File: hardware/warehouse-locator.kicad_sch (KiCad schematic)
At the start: 8 parts, among them J1 Screw_Terminal_01x03, J2 Screw_Terminal_01x03, J3 Screw_Terminal_01x03, J4 Barrel_Jack, J5 Screw_Terminal_01x03, J6 Screw_Terminal_01x03, J7 Screw_Terminal_01x03, U1 ESP32-DevKitC

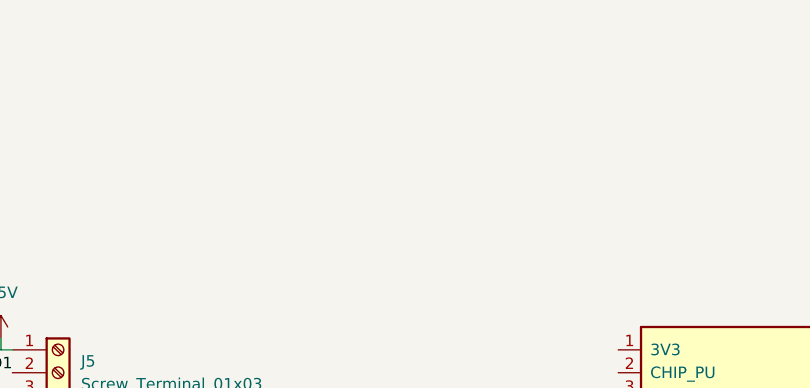
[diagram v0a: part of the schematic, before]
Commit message: Ethernet header
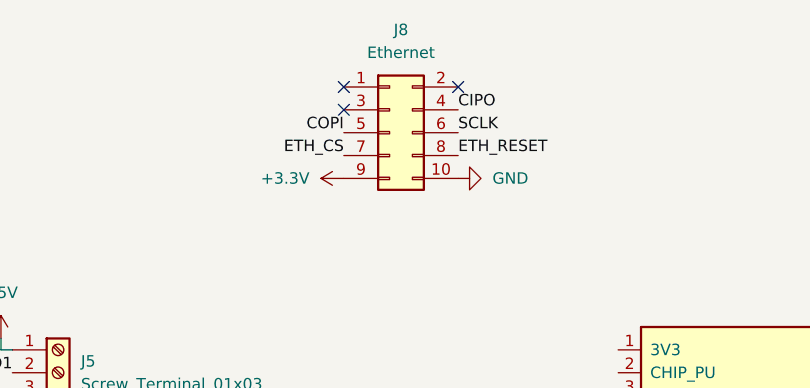
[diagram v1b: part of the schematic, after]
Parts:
- added J8: Ethernet, Connector_PinSocket_2.54mm:PinSocket_2x05_P2.54mm_Vertical, symbol Connector_Generic:Conn_02x05_Odd_Even
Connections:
- net GND: now also J8.10 (Pin_10)
- new net +3.3V: J8.9 (Pin_9)
- new net CIPO: J8.4 (Pin_4)
- new net COPI: J8.5 (Pin_5)
- new net ETH_CS: J8.7 (Pin_7)
- new net ETH_RESET: J8.8 (Pin_8)
- new net SCLK: J8.6 (Pin_6)
- no-connect marks 0 -> 3
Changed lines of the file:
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@@
 (kicad_sch (version 20211123) (generator eeschema)
   (paper "A4")
+  (no_connect (at 134.62 54.61))
+  (no_connect (at 134.62 52.07))
+  (no_connect (at 147.32 52.07))
   (wire (pts (xy 96.52 81.28) (xy 97.79 81.28))
     (stroke (width 0) (type default) (color 0 0 0 0))
@@
     (effects (font (size 1.27 1.27)) (justify right bottom))
   )
+  (label "ETH_RESET" (at 147.32 59.69 0)
+    (effects (font (size 1.27 1.27)) (justify left bottom))
+  )
+  (label "ETH_CS" (at 134.62 59.69 180)
+    (effects (font (size 1.27 1.27)) (justify right bottom))
+  )
+  (label "CIPO" (at 147.32 54.61 0)
+    (effects (font (size 1.27 1.27)) (justify left bottom))
+  )
   (label "LED0" (at 60.96 83.82 180)
     (effects (font (size 1.27 1.27)) (justify right bottom))
@@
   (label "LED5" (at 97.79 127 180)
     (effects (font (size 1.27 1.27)) (justify right bottom))
+  )
+  (label "COPI" (at 134.62 57.15 180)
+    (effects (font (size 1.27 1.27)) (justify right bottom))
+  )
+  (label "SCLK" (at 147.32 57.15 0)
+    (effects (font (size 1.27 1.27)) (justify left bottom))
+  )
+  (symbol (lib_id "power:+3.3V") (at 134.62 62.23 90) (unit 1)
+    (in_bom yes) (on_board yes) (fields_autoplaced)
+    (property "Reference" "#PWR015" (id 0) (at 138.43 62.23 0)
+      (effects (font (size 1.27 1.27)) hide)
+    )
+    (property "Value" "+3.3V" (id 1) (at 130.81 62.2299 90)
+      (effects (font (size 1.27 1.27)) (justify left))
+    )
+    (property "Footprint" "" (id 2) (at 134.62 62.23 0)
+      (effects (font (size 1.27 1.27)) hide)
+    )
+    (property "Datasheet" "" (id 3) (at 134.62 62.23 0)
+      (effects (font (size 1.27 1.27)) hide)
+    )
+    (pin "1")
   )
   (symbol (lib_id "power:+5V") (at 96.52 80.01 0) (unit 1)
@@
     (pin "3")
   )
+  (symbol (lib_id "power:GND") (at 147.32 62.23 90) (unit 1)
+    (in_bom yes) (on_board yes) (fields_autoplaced)
+    (property "Reference" "#PWR016" (id 0) (at 153.67 62.23 0)
+      (effects (font (size 1.27 1.27)) hide)
+    )
+    (property "Value" "GND" (id 1) (at 151.13 62.2299 90)
+      (effects (font (size 1.27 1.27)) (justify right))
+    )
+    (property "Footprint" "" (id 2) (at 147.32 62.23 0)
+      (effects (font (size 1.27 1.27)) hide)
+    )
+    (property "Datasheet" "" (id 3) (at 147.32 62.23 0)
+      (effects (font (size 1.27 1.27)) hide)
+    )
+    (pin "1")
+  )
   (symbol (lib_id "Connector:Screw_Terminal_01x03") (at 102.87 127 0) (unit 1)
     (in_bom yes) (on_board yes) (fields_autoplaced)
@@
     )
     (pin "1")
+  )
+  (symbol (lib_id "Connector_Generic:Conn_02x05_Odd_Even") (at 139.7 57.15 0) (unit 1)
+    (in_bom yes) (on_board yes) (fields_autoplaced)
+    (property "Reference" "J8" (id 0) (at 140.97 45.72 0))
+    (property "Value" "Ethernet" (id 1) (at 140.97 48.26 0))
+    (property "Footprint" "Connector_PinSocket_2.54mm:PinSocket_2x05_P2.54mm_Vertical" (id 2) (at 139.7 57.15 0)
+      (effects (font (size 1.27 1.27)) hide)
+    )
+    (property "Datasheet" "~" (id 3) (at 139.7 57.15 0)
+      (effects (font (size 1.27 1.27)) hide)
+    )
+    (pin "1")
+    (pin "10")
+    (pin "2")
+    (pin "3")
+    (pin "4")
+    (pin "5")
+    (pin "6")
+    (pin "7")
+    (pin "8")
+    (pin "9")
   )
   (symbol (lib_id "power:GND") (at 59.69 109.22 0) (unit 1)
@@
       (reference "#PWR014") (unit 1) (value "GND") (footprint "")
     )
+    (path "/053d9fce-626c-4602-916b-ef89efbc2685"
+      (reference "#PWR015") (unit 1) (value "+3.3V") (footprint "")
+    )
+    (path "/c6e94d68-e716-4c42-b935-ba265a888be2"
+      (reference "#PWR016") (unit 1) (value "GND") (footprint "")
+    )
     (path "/3aaacb84-122f-4340-95d3-0bf04eee80d2"
       (reference "J1") (unit 1) (value "Screw_Terminal_01x03") (footprint "TerminalBlock_Phoenix:TerminalBlock_Phoenix_MKDS-1,5-3_1x03_P5.00mm_Horizontal")
@@
       (reference "J7") (unit 1) (value "Screw_Terminal_01x03") (footprint "TerminalBlock_Phoenix:TerminalBlock_Phoenix_MKDS-1,5-3_1x03_P5.00mm_Horizontal")
     )
+    (path "/df94ba07-cbc6-4baa-93b8-732ae39550c6"
+      (reference "J8") (unit 1) (value "Ethernet") (footprint "Connector_PinSocket_2.54mm:PinSocket_2x05_P2.54mm_Vertical")
+    )
     (path "/8a6d48a6-b7bb-4a02-b51b-9f669ac7dca2"

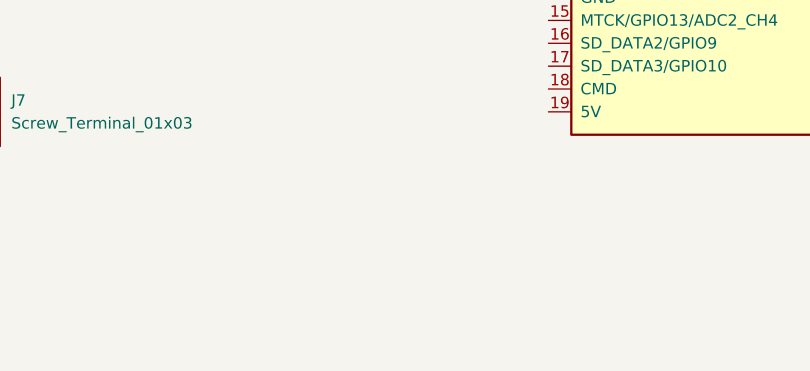
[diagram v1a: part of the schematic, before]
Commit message: Component positioning
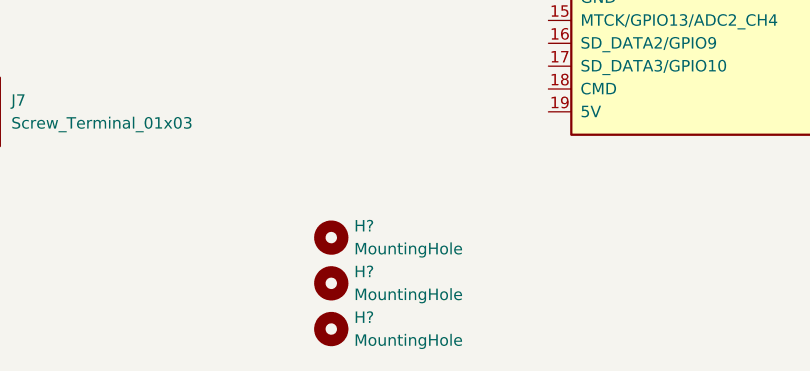
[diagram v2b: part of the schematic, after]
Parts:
- added H? (x3): MountingHole, MountingHole:MountingHole_3.2mm_M3_DIN965_Pad, symbol Mechanical:MountingHole
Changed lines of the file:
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@@
     (pin "3")
+  )
+  (symbol (lib_id "Mechanical:MountingHole") (at 140.97 140.97 0) (unit 1)
+    (in_bom yes) (on_board yes) (fields_autoplaced)
+    (property "Reference" "H?" (id 0) (at 143.51 139.6999 0)
+      (effects (font (size 1.27 1.27)) (justify left))
+    )
+    (property "Value" "MountingHole" (id 1) (at 143.51 142.2399 0)
+      (effects (font (size 1.27 1.27)) (justify left))
+    )
+    (property "Footprint" "MountingHole:MountingHole_3.2mm_M3_DIN965_Pad" (id 2) (at 140.97 140.97 0)
+      (effects (font (size 1.27 1.27)) hide)
+    )
+    (property "Datasheet" "~" (id 3) (at 140.97 140.97 0)
+      (effects (font (size 1.27 1.27)) hide)
+    )
   )
   (symbol (lib_id "power:+5V") (at 59.69 101.6 0) (unit 1)
@@
     (pin "1")
   )
+  (symbol (lib_id "Mechanical:MountingHole") (at 140.97 151.13 0) (unit 1)
+    (in_bom yes) (on_board yes) (fields_autoplaced)
+    (property "Reference" "H?" (id 0) (at 143.51 149.8599 0)
+      (effects (font (size 1.27 1.27)) (justify left))
+    )
+    (property "Value" "MountingHole" (id 1) (at 143.51 152.3999 0)
+      (effects (font (size 1.27 1.27)) (justify left))
+    )
+    (property "Footprint" "MountingHole:MountingHole_3.2mm_M3_DIN965_Pad" (id 2) (at 140.97 151.13 0)
+      (effects (font (size 1.27 1.27)) hide)
+    )
+    (property "Datasheet" "~" (id 3) (at 140.97 151.13 0)
+      (effects (font (size 1.27 1.27)) hide)
+    )
+  )
   (symbol (lib_id "Connector:Screw_Terminal_01x03") (at 66.04 127 0) (unit 1)
     (in_bom yes) (on_board yes) (fields_autoplaced)
@@
     (pin "2")
     (pin "3")
+  )
+  (symbol (lib_id "Mechanical:MountingHole") (at 140.97 146.05 0) (unit 1)
+    (in_bom yes) (on_board yes) (fields_autoplaced)
+    (property "Reference" "H?" (id 0) (at 143.51 144.7799 0)
+      (effects (font (size 1.27 1.27)) (justify left))
+    )
+    (property "Value" "MountingHole" (id 1) (at 143.51 147.3199 0)
+      (effects (font (size 1.27 1.27)) (justify left))
+    )
+    (property "Footprint" "MountingHole:MountingHole_3.2mm_M3_DIN965_Pad" (id 2) (at 140.97 146.05 0)
+      (effects (font (size 1.27 1.27)) hide)
+    )
+    (property "Datasheet" "~" (id 3) (at 140.97 146.05 0)
+      (effects (font (size 1.27 1.27)) hide)
+    )
   )
   (symbol (lib_id "Connector:Screw_Terminal_01x03") (at 66.04 105.41 0) (unit 1)
@@
       (reference "#PWR016") (unit 1) (value "GND") (footprint "")
     )
+    (path "/3f6f5fd4-bf84-4f5a-b527-b698f4821ee8"
+      (reference "H?") (unit 1) (value "MountingHole") (footprint "MountingHole:MountingHole_3.2mm_M3_DIN965_Pad")
+    )
+    (path "/a523383e-b510-4a6d-92cb-0d2f830ea5c3"
+      (reference "H?") (unit 1) (value "MountingHole") (footprint "MountingHole:MountingHole_3.2mm_M3_DIN965_Pad")
+    )
+    (path "/a915c05e-ae38-4c6d-9a9c-84e50169004a"
+      (reference "H?") (unit 1) (value "MountingHole") (footprint "MountingHole:MountingHole_3.2mm_M3_DIN965_Pad")
+    )
     (path "/3aaacb84-122f-4340-95d3-0bf04eee80d2"

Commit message: Pins connected
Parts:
- gave numbers to parts that had none: 3
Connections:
- net +3.3V: now also U1.1 (3V3)
- net +5V: now also U1.19 (5V)
- net CIPO: now also U1.31 (GPIO19)
- net COPI: now also U1.37 (GPIO23)
- net ETH_CS: now also U1.29 (*GPIO5)
- net GND: now also U1.14 (GND), U1.32 (GND), U1.38 (GND)
- net LED0: now also U1.33 (GPIO21)
- net LED1: now also U1.28 (GPIO17)
- net LED2: now also U1.26 (ADC2_CH0/GPIO4)
- net LED3: now also U1.36 (GPIO22)
- net LED4: now also U1.27 (GPIO16)
- net LED5: now also U1.24 (ADC2_CH2/*GPIO2)
- net SCLK: now also U1.30 (GPIO18)
- net ETH_RESET: no longer names the net of J8.8 (Pin_8)
- no-connect marks 3 -> 27
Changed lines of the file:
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@@
 (kicad_sch (version 20211123) (generator eeschema)
   (paper "A4")
+  (no_connect (at 165.1 116.84))
+  (no_connect (at 233.68 124.46))
+  (no_connect (at 165.1 119.38))
+  (no_connect (at 165.1 83.82))
   (no_connect (at 134.62 54.61))
+  (no_connect (at 165.1 99.06))
   (no_connect (at 134.62 52.07))
+  (no_connect (at 165.1 124.46))
+  (no_connect (at 233.68 127))
+  (no_connect (at 233.68 121.92))
+  (no_connect (at 165.1 93.98))
+  (no_connect (at 165.1 121.92))
+  (no_connect (at 165.1 104.14))
+  (no_connect (at 165.1 91.44))
+  (no_connect (at 233.68 114.3))
+  (no_connect (at 233.68 119.38))
+  (no_connect (at 165.1 86.36))
+  (no_connect (at 233.68 91.44))
+  (no_connect (at 165.1 101.6))
+  (no_connect (at 165.1 96.52))
+  (no_connect (at 165.1 88.9))
+  (no_connect (at 147.32 59.69))
+  (no_connect (at 165.1 111.76))
   (no_connect (at 147.32 52.07))
+  (no_connect (at 165.1 109.22))
+  (no_connect (at 165.1 106.68))
+  (no_connect (at 233.68 88.9))
   (wire (pts (xy 96.52 81.28) (xy 97.79 81.28))
     (stroke (width 0) (type default) (color 0 0 0 0))
@@
     (stroke (width 0) (type default) (color 0 0 0 0))
   )
+  (wire (pts (xy 238.76 96.52) (xy 233.68 96.52))
+    (stroke (width 0) (type default) (color 0 0 0 0))
+  )
   (wire (pts (xy 96.52 101.6) (xy 96.52 102.87))
     (stroke (width 0) (type default) (color 0 0 0 0))
@@
   )
   (wire (pts (xy 59.69 129.54) (xy 60.96 129.54))
+    (stroke (width 0) (type default) (color 0 0 0 0))
+  )
+  (wire (pts (xy 238.76 81.28) (xy 233.68 81.28))
     (stroke (width 0) (type default) (color 0 0 0 0))
   )
@@
     (effects (font (size 1.27 1.27)) (justify right bottom))
   )
+  (label "LED1" (at 233.68 106.68 0)
+    (effects (font (size 1.27 1.27)) (justify left bottom))
+  )
+  (label "LED0" (at 233.68 93.98 0)
+    (effects (font (size 1.27 1.27)) (justify left bottom))
+  )
   (label "LED3" (at 97.79 105.41 180)
     (effects (font (size 1.27 1.27)) (justify right bottom))
   )
+  (label "CIPO" (at 233.68 99.06 0)
+    (effects (font (size 1.27 1.27)) (justify left bottom))
+  )
   (label "LED1" (at 97.79 83.82 180)
     (effects (font (size 1.27 1.27)) (justify right bottom))
@@
     (effects (font (size 1.27 1.27)) (justify right bottom))
   )
-  (label "ETH_RESET" (at 147.32 59.69 0)
+  (label "LED2" (at 233.68 111.76 0)
+    (effects (font (size 1.27 1.27)) (justify left bottom))
+  )
+  (label "LED4" (at 233.68 109.22 0)
     (effects (font (size 1.27 1.27)) (justify left bottom))
   )
@@
     (effects (font (size 1.27 1.27)) (justify left bottom))
   )
+  (label "COPI" (at 233.68 83.82 0)
+    (effects (font (size 1.27 1.27)) (justify left bottom))
+  )
   (label "LED0" (at 60.96 83.82 180)
     (effects (font (size 1.27 1.27)) (justify right bottom))
   )
+  (label "SCLK" (at 233.68 101.6 0)
+    (effects (font (size 1.27 1.27)) (justify left bottom))
+  )
+  (label "LED5" (at 233.68 116.84 0)
+    (effects (font (size 1.27 1.27)) (justify left bottom))
+  )
+  (label "LED3" (at 233.68 86.36 0)
+    (effects (font (size 1.27 1.27)) (justify left bottom))
+  )
   (label "LED5" (at 97.79 127 180)
     (effects (font (size 1.27 1.27)) (justify right bottom))
   )
+  (label "ETH_CS" (at 233.68 104.14 0)
+    (effects (font (size 1.27 1.27)) (justify left bottom))
+  )
   (label "COPI" (at 134.62 57.15 180)
     (effects (font (size 1.27 1.27)) (justify right bottom))
@@
     (effects (font (size 1.27 1.27)) (justify left bottom))
   )
+  (symbol (lib_id "power:+5V") (at 165.1 127 90) (unit 1)
+    (in_bom yes) (on_board yes)
+    (property "Reference" "#PWR?" (id 0) (at 168.91 127 0)
+      (effects (font (size 1.27 1.27)) hide)
+    )
+    (property "Value" "+5V" (id 1) (at 157.48 127 90)
+      (effects (font (size 1.27 1.27)) (justify right))
+    )
+    (property "Footprint" "" (id 2) (at 165.1 127 0)
+      (effects (font (size 1.27 1.27)) hide)
+    )
+    (property "Datasheet" "" (id 3) (at 165.1 127 0)
+      (effects (font (size 1.27 1.27)) hide)
+    )
+    (pin "1")
+  )
   (symbol (lib_id "power:+3.3V") (at 134.62 62.23 90) (unit 1)
     (in_bom yes) (on_board yes) (fields_autoplaced)
@@
     )
     (property "Datasheet" "" (id 3) (at 134.62 62.23 0)
+      (effects (font (size 1.27 1.27)) hide)
+    )
+    (pin "1")
+  )
+  (symbol (lib_name "GND_2") (lib_id "power:GND") (at 165.1 114.3 270) (unit 1)
+    (in_bom yes) (on_board yes) (fields_autoplaced)
+    (property "Reference" "#PWR?" (id 0) (at 158.75 114.3 0)
+      (effects (font (size 1.27 1.27)) hide)
+    )
+    (property "Value" "GND" (id 1) (at 161.29 114.2999 90)
+      (effects (font (size 1.27 1.27)) (justify right))
+    )
+    (property "Footprint" "" (id 2) (at 165.1 114.3 0)
+      (effects (font (size 1.27 1.27)) hide)
+    )
+    (property "Datasheet" "" (id 3) (at 165.1 114.3 0)
       (effects (font (size 1.27 1.27)) hide)
     )
@@
     (pin "3")
   )
+  (symbol (lib_name "GND_1") (lib_id "power:GND") (at 238.76 81.28 90) (unit 1)
+    (in_bom yes) (on_board yes) (fields_autoplaced)
+    (property "Reference" "#PWR?" (id 0) (at 245.11 81.28 0)
+      (effects (font (size 1.27 1.27)) hide)
+    )
+    (property "Value" "GND" (id 1) (at 242.57 81.2799 90)
+      (effects (font (size 1.27 1.27)) (justify right))
+    )
+    (property "Footprint" "" (id 2) (at 238.76 81.28 0)
+      (effects (font (size 1.27 1.27)) hide)
+    )
+    (property "Datasheet" "" (id 3) (at 238.76 81.28 0)
+      (effects (font (size 1.27 1.27)) hide)
+    )
+    (pin "1")
+  )
   (symbol (lib_id "Connector:Screw_Terminal_01x03") (at 66.04 83.82 0) (unit 1)
     (in_bom yes) (on_board yes) (fields_autoplaced)
@@
   (symbol (lib_id "Mechanical:MountingHole") (at 140.97 140.97 0) (unit 1)
     (in_bom yes) (on_board yes) (fields_autoplaced)
-    (property "Reference" "H?" (id 0) (at 143.51 139.6999 0)
+    (property "Reference" "H1" (id 0) (at 143.51 139.6999 0)
       (effects (font (size 1.27 1.27)) (justify left))
     )
@@
   (symbol (lib_id "Mechanical:MountingHole") (at 140.97 151.13 0) (unit 1)
     (in_bom yes) (on_board yes) (fields_autoplaced)
-    (property "Reference" "H?" (id 0) (at 143.51 149.8599 0)
+    (property "Reference" "H3" (id 0) (at 143.51 149.8599 0)
       (effects (font (size 1.27 1.27)) (justify left))
     )
@@
   (symbol (lib_id "Mechanical:MountingHole") (at 140.97 146.05 0) (unit 1)
     (in_bom yes) (on_board yes) (fields_autoplaced)
-    (property "Reference" "H?" (id 0) (at 143.51 144.7799 0)
+    (property "Reference" "H2" (id 0) (at 143.51 144.7799 0)
       (effects (font (size 1.27 1.27)) (justify left))
     )
@@
     (pin "2")
     (pin "3")
+  )
+  (symbol (lib_name "GND_1") (lib_id "power:GND") (at 238.76 96.52 90) (unit 1)
+    (in_bom yes) (on_board yes) (fields_autoplaced)
+    (property "Reference" "#PWR?" (id 0) (at 245.11 96.52 0)
+      (effects (font (size 1.27 1.27)) hide)
+    )
+    (property "Value" "GND" (id 1) (at 242.57 96.5199 90)
+      (effects (font (size 1.27 1.27)) (justify right))
+    )
+    (property "Footprint" "" (id 2) (at 238.76 96.52 0)
+      (effects (font (size 1.27 1.27)) hide)
+    )
+    (property "Datasheet" "" (id 3) (at 238.76 96.52 0)
+      (effects (font (size 1.27 1.27)) hide)
+    )
+    (pin "1")
+  )
+  (symbol (lib_id "power:+3.3V") (at 165.1 81.28 90) (unit 1)
+    (in_bom yes) (on_board yes) (fields_autoplaced)
+    (property "Reference" "#PWR?" (id 0) (at 168.91 81.28 0)
+      (effects (font (size 1.27 1.27)) hide)
+    )
+    (property "Value" "+3.3V" (id 1) (at 161.29 81.2799 90)
+      (effects (font (size 1.27 1.27)) (justify left))
+    )
+    (property "Footprint" "" (id 2) (at 165.1 81.28 0)
+      (effects (font (size 1.27 1.27)) hide)
+    )
+    (property "Datasheet" "" (id 3) (at 165.1 81.28 0)
+      (effects (font (size 1.27 1.27)) hide)
+    )
+    (pin "1")
   )
   (symbol (lib_id "Connector:Screw_Terminal_01x03") (at 102.87 105.41 0) (unit 1)
@@
       (reference "#PWR016") (unit 1) (value "GND") (footprint "")
     )
+    (path "/0254aefe-66fc-4322-8d36-d41b0cd7ed4c"
+      (reference "#PWR?") (unit 1) (value "+5V") (footprint "")
+    )
+    (path "/0ff64a17-acbe-42e6-b6e4-0d8dd8c401b1"
+      (reference "#PWR?") (unit 1) (value "GND") (footprint "")
+    )
+    (path "/213ea978-248f-4385-b520-aff4ee3ab8b6"
+      (reference "#PWR?") (unit 1) (value "GND") (footprint "")
+    )
+    (path "/b6dc58df-5635-4bfb-a0b6-f31ca3e9691d"
+      (reference "#PWR?") (unit 1) (value "GND") (footprint "")
+    )
+    (path "/b8c97f6d-2826-4abe-9a0d-fbf24acc9464"
+      (reference "#PWR?") (unit 1) (value "+3.3V") (footprint "")
+    )
     (path "/3f6f5fd4-bf84-4f5a-b527-b698f4821ee8"
-      (reference "H?") (unit 1) (value "MountingHole") (footprint "MountingHole:MountingHole_3.2mm_M3_DIN965_Pad")
+      (reference "H1") (unit 1) (value "MountingHole") (footprint "MountingHole:MountingHole_3.2mm_M3_DIN965_Pad")
+    )
+    (path "/a915c05e-ae38-4c6d-9a9c-84e50169004a"
+      (reference "H2") (unit 1) (value "MountingHole") (footprint "MountingHole:MountingHole_3.2mm_M3_DIN965_Pad")
     )
     (path "/a523383e-b510-4a6d-92cb-0d2f830ea5c3"
-      (reference "H?") (unit 1) (value "MountingHole") (footprint "MountingHole:MountingHole_3.2mm_M3_DIN965_Pad")
-    )
-    (path "/a915c05e-ae38-4c6d-9a9c-84e50169004a"
-      (reference "H?") (unit 1) (value "MountingHole") (footprint "MountingHole:MountingHole_3.2mm_M3_DIN965_Pad")
+      (reference "H3") (unit 1) (value "MountingHole") (footprint "MountingHole:MountingHole_3.2mm_M3_DIN965_Pad")
     )
     (path "/3aaacb84-122f-4340-95d3-0bf04eee80d2"
